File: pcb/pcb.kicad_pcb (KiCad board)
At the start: 2 copper layers, 141.5 x 81.4 mm, 29 parts, among them J1 Screw_Terminal_01x02, J2 Screw_Terminal_01x02, K00 Kailh Choc, K01 Kailh Choc, K02 Kailh Choc, K10 Kailh Choc, K11 Kailh Choc, K12 Kailh Choc, K20 Kailh Choc, K21 Kailh Choc, K22 Kailh Choc, K23 Kailh Choc, K30 Kailh Choc, K31 Kailh Choc, K32 Kailh Choc, K33 Kailh Choc, K40 Kailh Choc, K41 Kailh Choc, K42 Kailh Choc, K43 Kailh Choc, K50 Kailh Choc, K51 Kailh Choc, K52 Kailh Choc, K53 Kailh Choc, K60 Kailh Choc, SW1 SW_DPST, SW2 SW_Push_DPDT, SW3 SW_Push_DPDT, U1 nice_nano

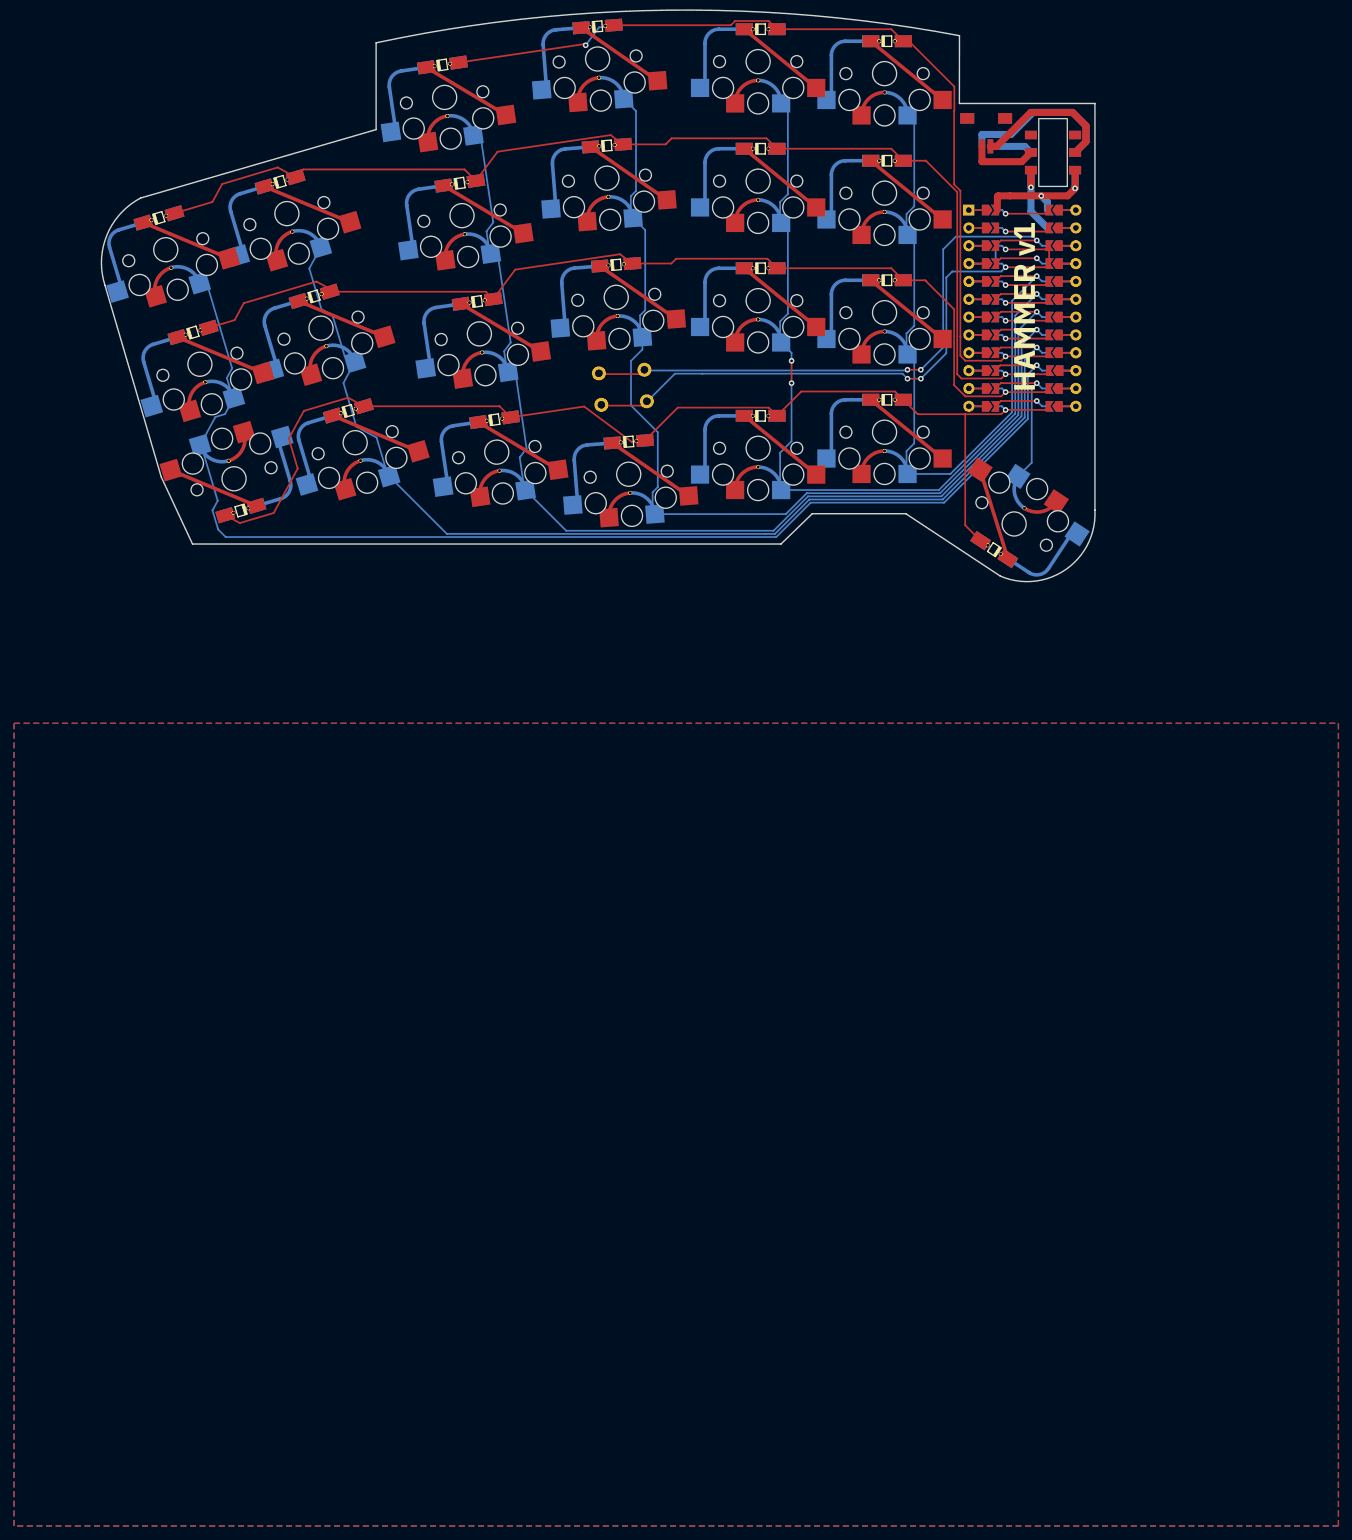
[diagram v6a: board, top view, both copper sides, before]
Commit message: update pcb for low pro battery connector
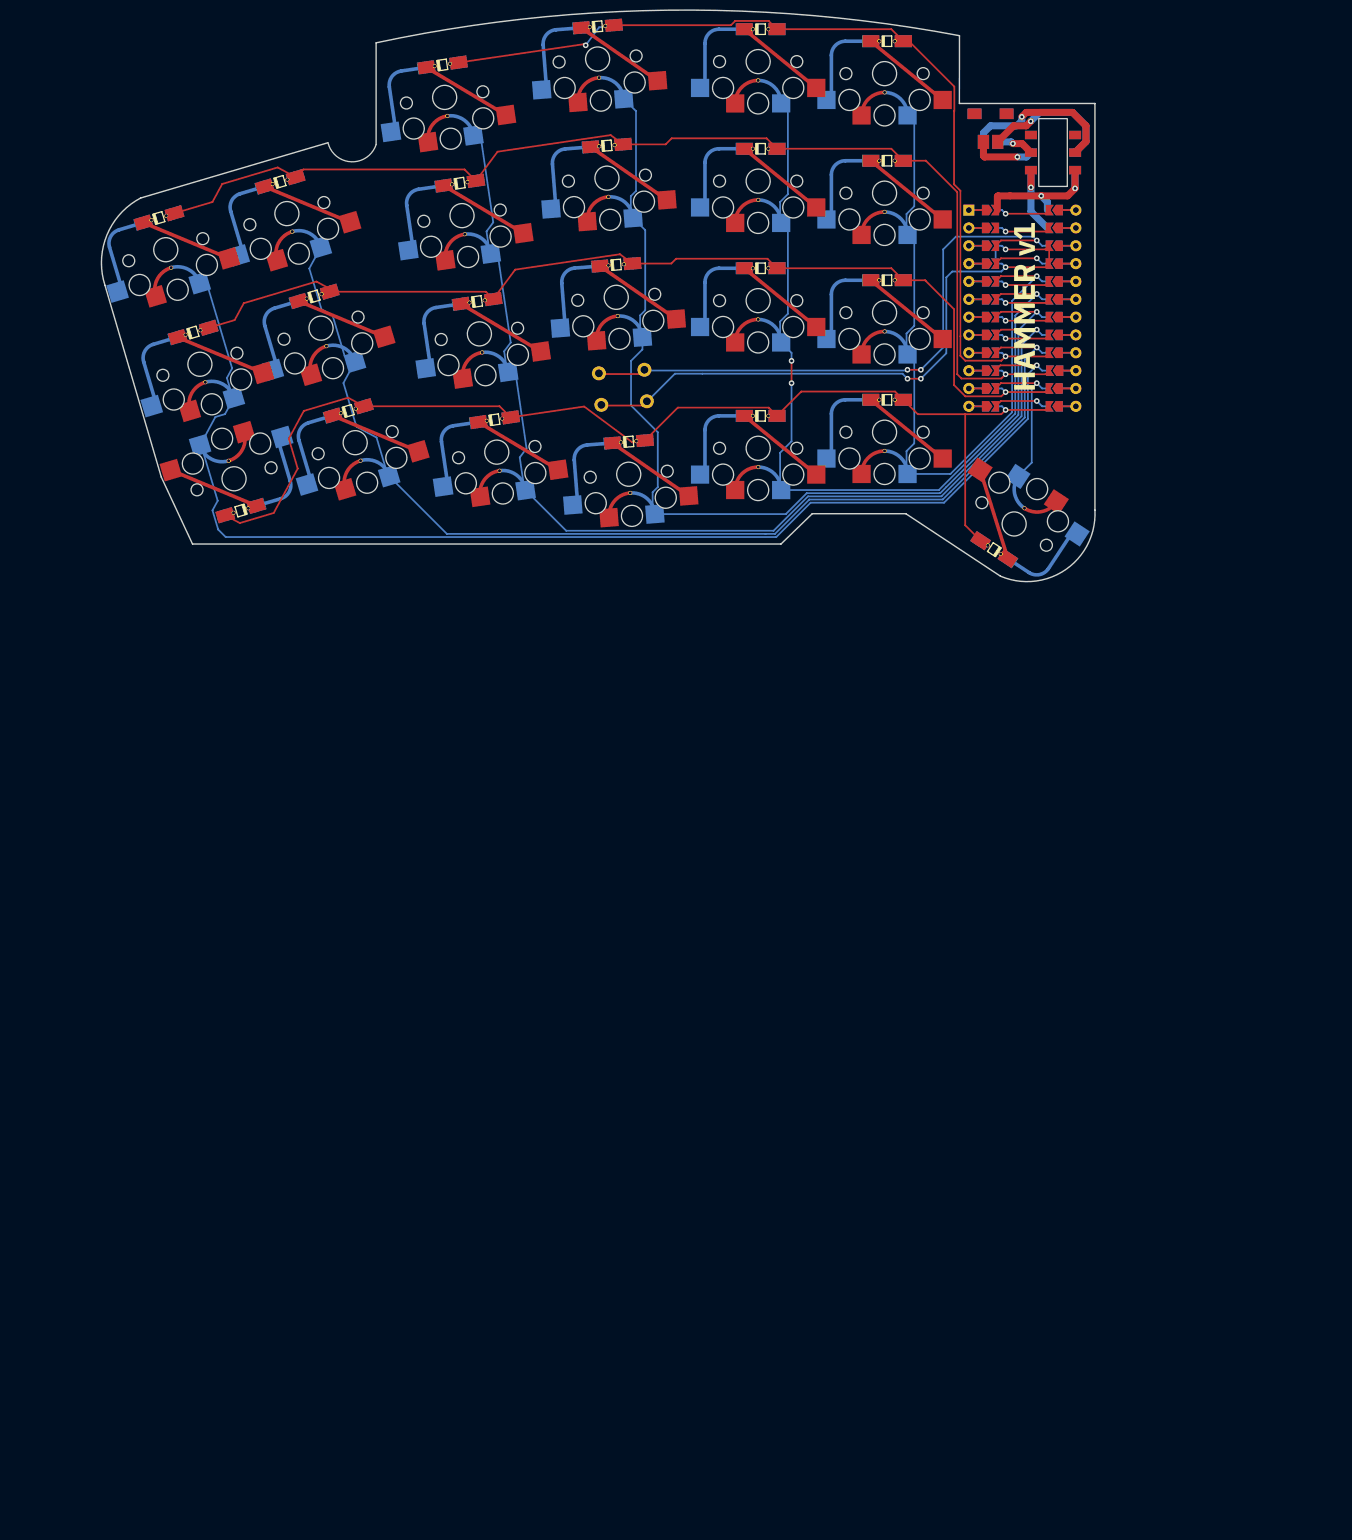
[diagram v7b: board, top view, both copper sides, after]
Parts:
- J1: moved to B.Cu
- J2: moved to F.Cu
- moved J1 0.90 mm to (194.9, 64.1)
- moved J2 0.90 mm to (194.9, 64.1)
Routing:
- net Net-(J1-Pad1): track 9.70 -> 5.36 mm, vias 0 -> 1
- net Net-(J2-Pad2): track 23.1 -> 19.5 mm, vias 0 -> 1
- net Net-(J2-Pad1): track 6.14 -> 9.09 mm, vias 0 -> 1
- net Net-(J1-Pad2): track 20.9 -> 22.7 mm, vias 0 -> 1
- removed copper zone on B.Cu, net GND
- removed copper zone on F.Cu, net GND
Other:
- outline, holes or cut-outs redrawn

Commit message: pcb v1
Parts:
- added G***: LOGO, lib:friends5, F.Cu at (198.6, 67.4)
- added G***: LOGO, lib:friends5, B.Cu at (91.4, 73.7)
